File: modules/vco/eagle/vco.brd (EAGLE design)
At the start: 100 x 87.6 mm, 115 parts, among them IC1 TL074P, IC2 TL072P, IC3 TL072P, IC4 TL072P, IC5 TL072P, Q1 J107, T1 2N3904, T2 2N3904, T3 2N3904, T4 2N3904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

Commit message: VCO PCB fixes
- Fixes a couple of design flaws: two opamps hade the inputs the wrong way
  around, the sine output net intersected with a pin connected to ground
- Moves the connector legend to the tName layer so they show up in fab.
- Adds legends to the trimpots
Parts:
- moved R20 2.54 mm to (61.0, 63.5)
- moved R21 2.54 mm to (61.0, 61.0)
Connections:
- net GND: now also IC2.5; no longer IC2.6
- net N$22: now also IC2.2; no longer IC2.3
- net N$25: now also IC2.3; no longer IC2.2
- net N$26: now also IC2.6; no longer IC2.5
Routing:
- net GND: track 14.3 -> 5.08 mm
- net N$26: track 5.08 -> 9.57 mm
- net N$SAW-OUT1: track 133.8 -> 129.5 mm
- net N$14: track 46.7 -> 44.2 mm
- net N$SINE-OUT1: track 28.5 -> 27.0 mm
- net N$25: track 8.89 -> 9.94 mm
- added copper zone on layer 16, net GND
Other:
- board text added: "HIGH FREQ"
- board text added: "SAW OFFSET"
- board text added: "SINE ROUNDNESS"
- board text added: "SINE SYMMETRY"
- board text added: "TRI OFFSET"

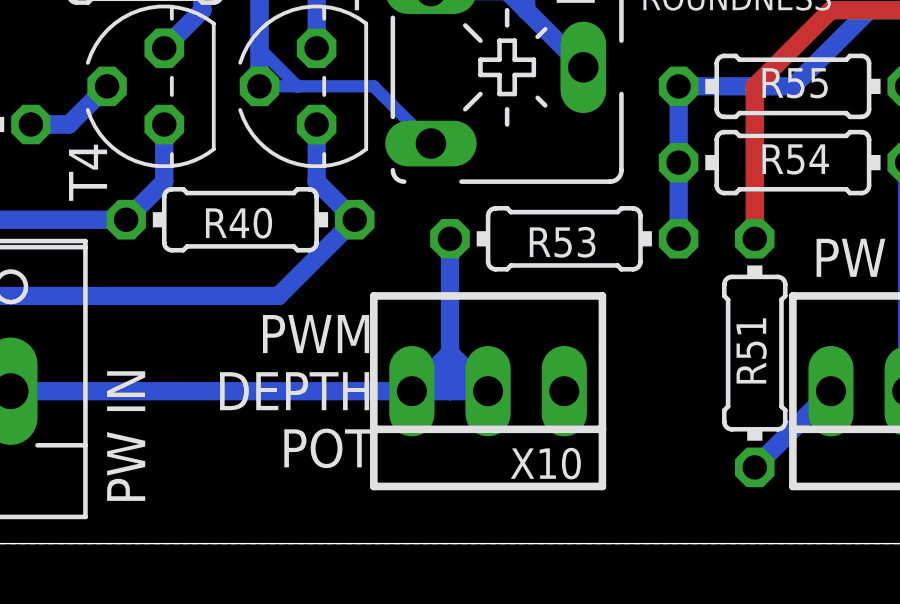
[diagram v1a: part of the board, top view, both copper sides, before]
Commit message: Fix pwm amount input on VCO
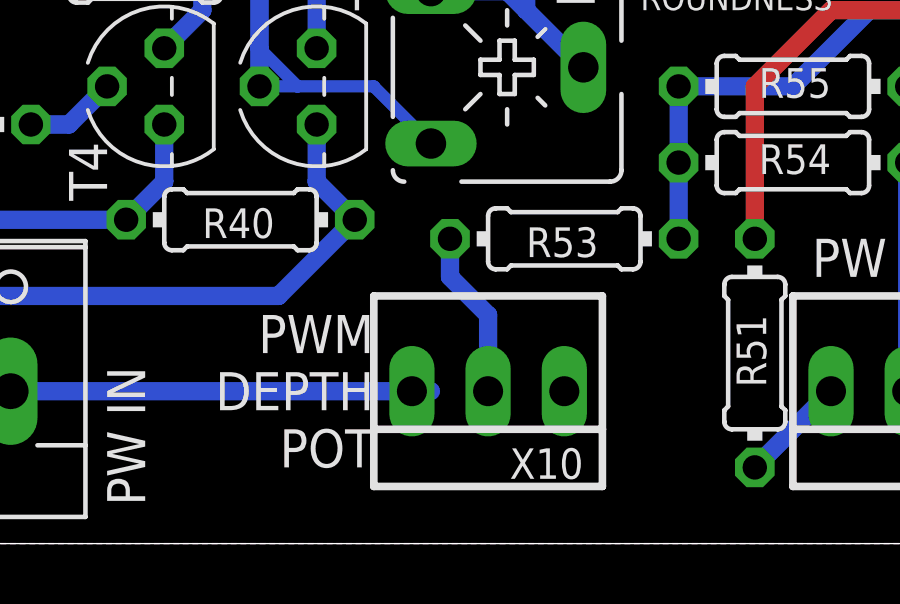
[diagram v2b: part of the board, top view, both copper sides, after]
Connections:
- new net N$65: R53.1, X10.2
- net N$49: no longer R53.1, X10.2
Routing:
- net N$49: track 27.0 -> 14.0 mm
- net N$65: track 0.00 -> 5.61 mm
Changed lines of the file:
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@@
 </signal>
 <signal name="N$49">
-<contactref element="X10" pad="2"/>
 <contactref element="X4" pad="2"/>
-<contactref element="R53" pad="1"/>
 <contactref element="X10" pad="3"/>
 <wire x1="36.155" y1="5.08" x2="49.53" y2="5.08" width="0.6096" layer="16"/>
-<wire x1="51.435" y1="5.08" x2="50.8" y2="5.08" width="0.6096" layer="16"/>
-<wire x1="50.8" y1="5.08" x2="49.53" y2="5.08" width="0.6096" layer="16"/>
-<wire x1="50.8" y1="10.16" x2="50.8" y2="6.35" width="0.6096" layer="16"/>
-<wire x1="50.8" y1="6.35" x2="50.8" y2="5.715" width="0.6096" layer="16"/>
-<wire x1="50.8" y1="5.715" x2="50.8" y2="5.08" width="0.6096" layer="16"/>
 <wire x1="49.53" y1="5.08" x2="50.165" y2="5.08" width="0.6096" layer="16"/>
-<wire x1="50.165" y1="5.08" x2="50.8" y2="5.715" width="0.6096" layer="16"/>
-<wire x1="50.8" y1="5.715" x2="51.435" y2="5.08" width="0.6096" layer="16"/>
-<wire x1="51.435" y1="5.08" x2="52.07" y2="5.08" width="0.6096" layer="16"/>
-<wire x1="52.07" y1="5.08" x2="50.8" y2="6.35" width="0.6096" layer="16"/>
-<wire x1="50.8" y1="6.35" x2="49.53" y2="5.08" width="0.6096" layer="16"/>
 </signal>
 <signal name="N$PW-CV1">
@@
 <via x="96.19" y="3.81" extent="1-16" drill="3.2" diameter="3.81"/>
 </signal>
+<signal name="N$65">
+<contactref element="X10" pad="2"/>
+<contactref element="R53" pad="1"/>
+<wire x1="50.8" y1="10.16" x2="50.8" y2="8.89" width="0.6096" layer="16"/>
+<wire x1="50.8" y1="8.89" x2="52.07" y2="7.62" width="0.6096" layer="16"/>
+<wire x1="52.07" y1="7.62" x2="52.07" y2="5.08" width="0.6096" layer="16"/>
+</signal>
 </signals>
